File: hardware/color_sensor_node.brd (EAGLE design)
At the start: 27.9 x 30.5 mm, 19 parts, among them J1 JTAG, J2 JTAG, U1 ISL29125, U2 3.3V, U3 WS2811

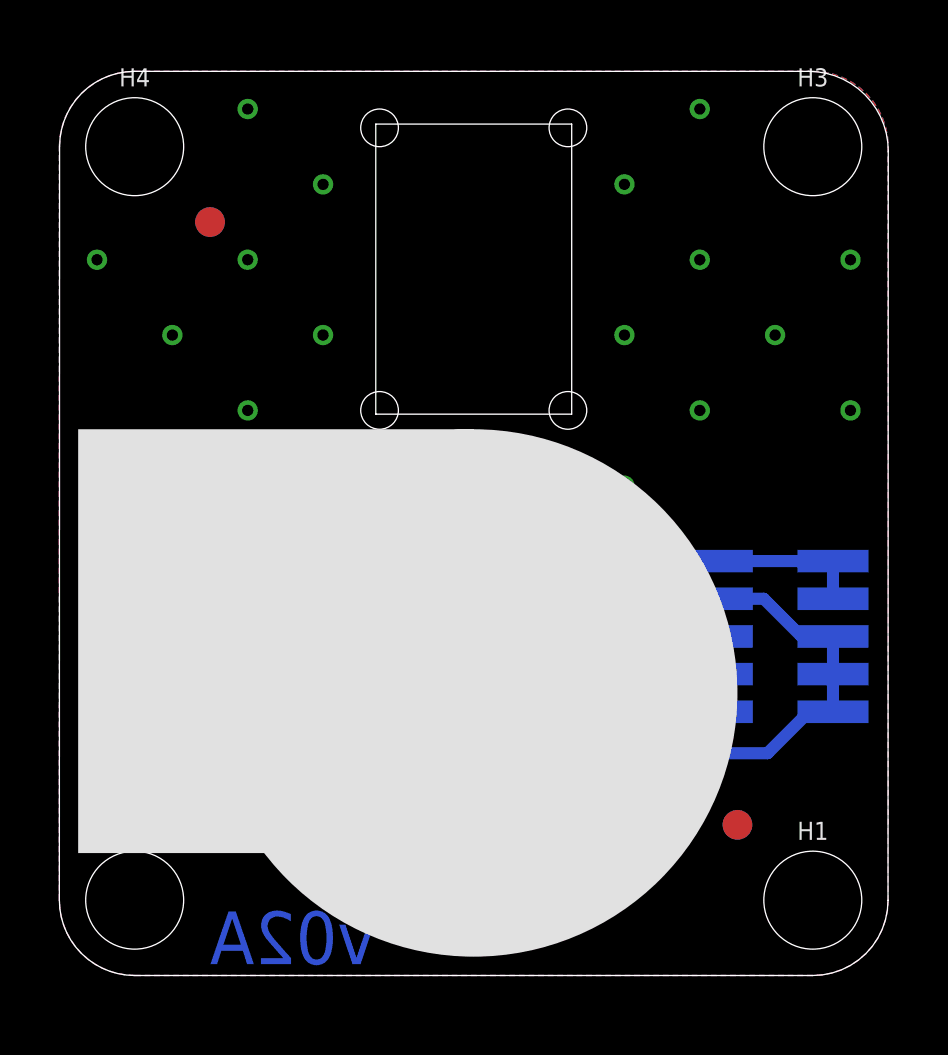
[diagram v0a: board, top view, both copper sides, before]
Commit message: update color sensor node board for after dark colors
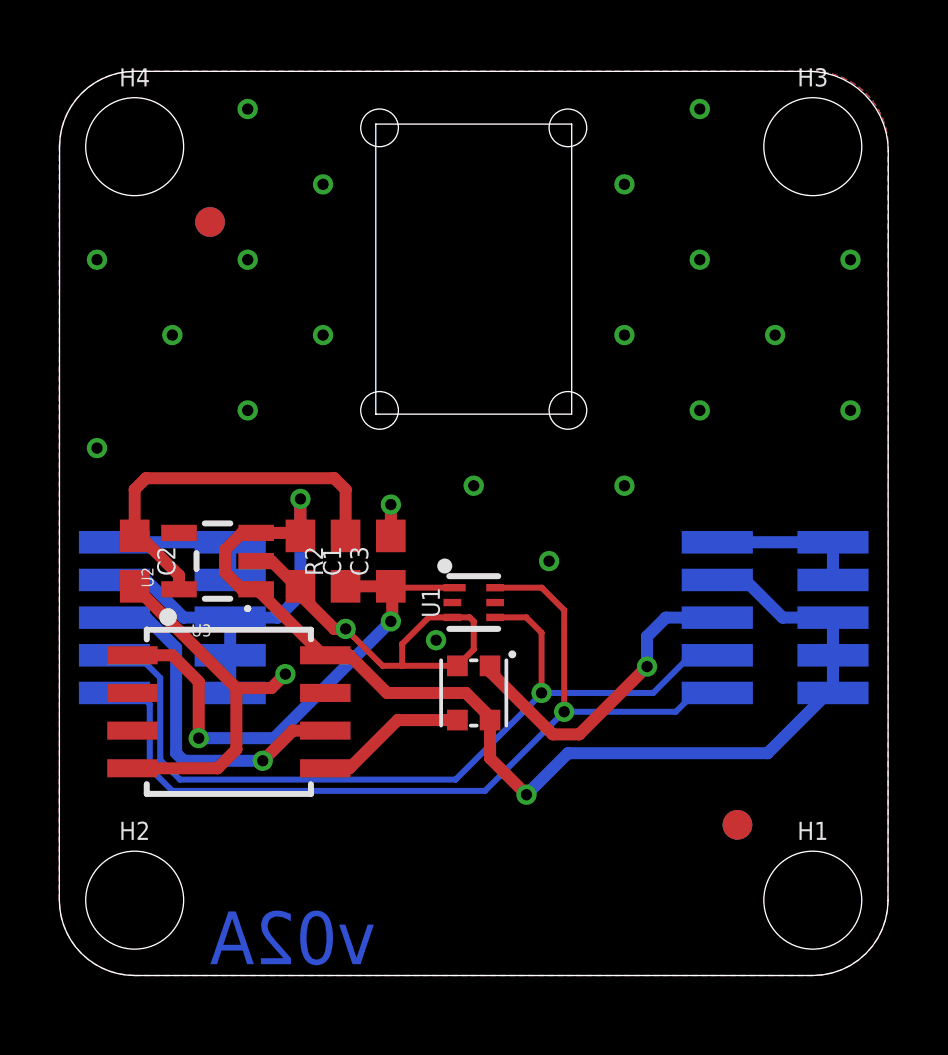
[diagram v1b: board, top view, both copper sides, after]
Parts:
- moved J1 0.63 mm to (3.81, 12.1)
- moved J2 0.63 mm to (24.1, 12.1)
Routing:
- net GND: track 24.1 -> 37.7 mm, vias 21 -> 23
- net SCL: track 29.5 -> 30.4 mm
- net DOUT: track 10.1 -> 11.0 mm
- net DIN: track 11.0 -> 11.6 mm
- net SDA: track 28.6 -> 29.2 mm
